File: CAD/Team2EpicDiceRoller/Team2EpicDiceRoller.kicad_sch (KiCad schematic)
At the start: 64 parts, among them J1 Conn_02x03_Odd_Even, J2 Conn_01x16, J3 Barrel_Jack, Q1 BSS138, SW1 SW_Toggle_SPDT, SW2 Tilt_Switch, SW3 SW_Power, SW4 RotaryEncoder_Switch, SW5 SW_LeftMenu, SW6 SW_MidMenu, SW7 SW_Reset, SW8 SW_RightMenu, U1 MC34063AD, U2 74HC14, U3 MC34063AD, U4 ATmega328P-P, Y1 Crystal_16MHz

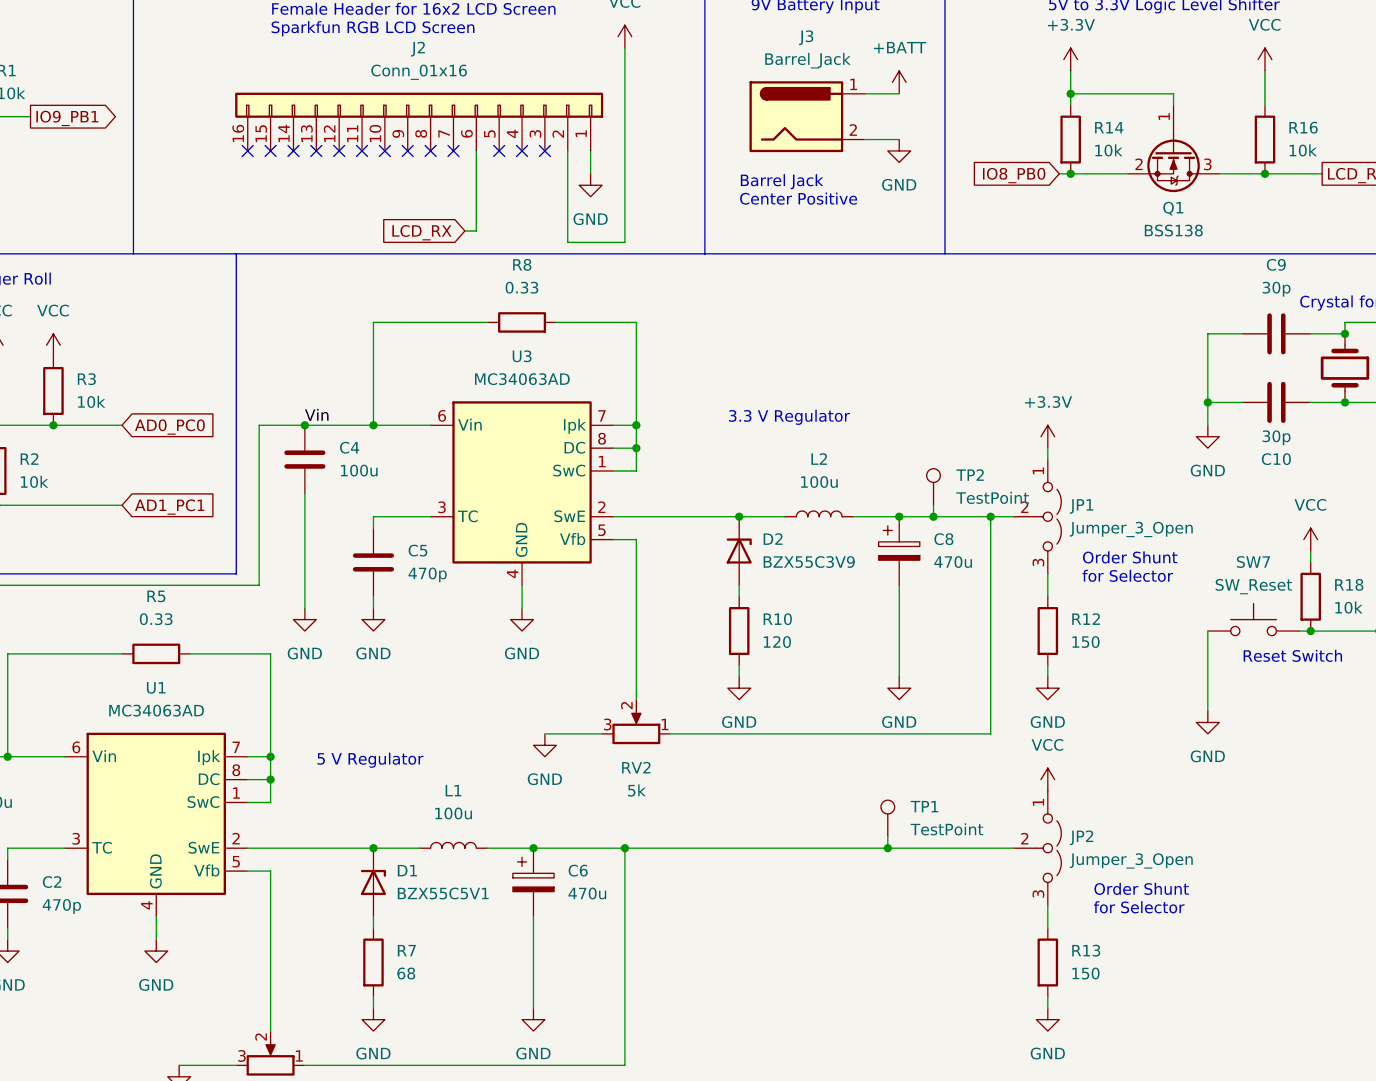
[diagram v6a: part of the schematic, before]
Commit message: Added mounting holes for the standoffs
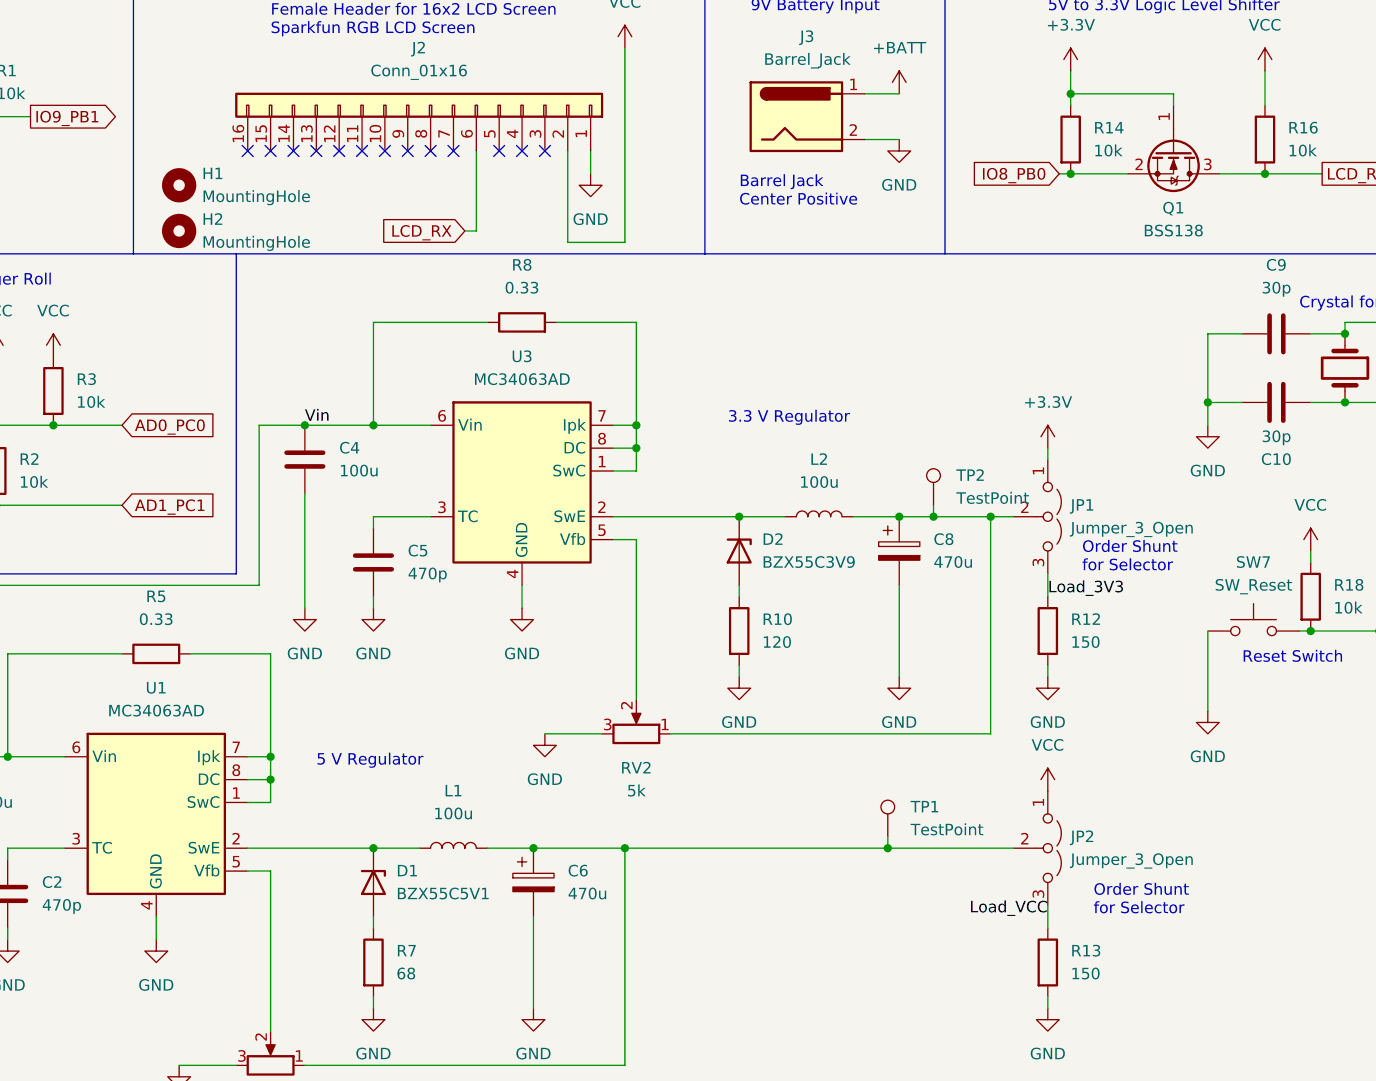
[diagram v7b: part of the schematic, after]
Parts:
- added H1, H2: MountingHole, MountingHole:MountingHole_3.2mm_M3, symbol Mechanical:MountingHole
- J2: footprint Connector_PinSocket_2.54mm:PinSocket_1x16_P2.54mm_Vertical -> Library:PinSocket_1x16_P2.54mm_Vertical_LCD
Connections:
- net Load_VCC: now reaches JP2.3 (B), R13.1
- net Load_3V3: now reaches JP1.3 (B), R12.1
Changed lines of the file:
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@@
     (effects (font (size 1.27 1.27)) (justify left bottom))
   )
-  (text "Order Shunt\nfor Selector" (at 158.75 137.16 0)
+  (text "Order Shunt\nfor Selector" (at 158.75 135.89 0)
     (effects (font (size 1.27 1.27)) (justify left bottom))
   )
@@
   (label "LeftDebn" (at 130.81 30.48 90)
     (effects (font (size 1.27 1.27)) (justify left bottom))
+  )
+  (label "Load_3V3" (at 154.94 138.43 0)
+    (effects (font (size 1.27 1.27)) (justify left bottom))
+  )
+  (label "Load_VCC" (at 154.94 173.99 180)
+    (effects (font (size 1.27 1.27)) (justify right bottom))
   )
   (label "MidDebn" (at 191.77 30.48 90)
@@
     (pin "1")
     (pin "2")
+  )
+  (symbol (lib_id "Mechanical:MountingHole") (at 58.42 92.71 0) (unit 1)
+    (in_bom yes) (on_board yes) (fields_autoplaced)
+    (property "Reference" "H1" (id 0) (at 60.96 91.4399 0)
+      (effects (font (size 1.27 1.27)) (justify left))
+    )
+    (property "Value" "MountingHole" (id 1) (at 60.96 93.9799 0)
+      (effects (font (size 1.27 1.27)) (justify left))
+    )
+    (property "Footprint" "MountingHole:MountingHole_3.2mm_M3" (id 2) (at 58.42 92.71 0)
+      (effects (font (size 1.27 1.27)) hide)
+    )
+    (property "Datasheet" "~" (id 3) (at 58.42 92.71 0)
+      (effects (font (size 1.27 1.27)) hide)
+    )
+  )
+  (symbol (lib_id "Mechanical:MountingHole") (at 58.42 97.79 0) (unit 1)
+    (in_bom yes) (on_board yes) (fields_autoplaced)
+    (property "Reference" "H2" (id 0) (at 60.96 96.5199 0)
+      (effects (font (size 1.27 1.27)) (justify left))
+    )
+    (property "Value" "MountingHole" (id 1) (at 60.96 99.0599 0)
+      (effects (font (size 1.27 1.27)) (justify left))
+    )
+    (property "Footprint" "MountingHole:MountingHole_3.2mm_M3" (id 2) (at 58.42 97.79 0)
+      (effects (font (size 1.27 1.27)) hide)
+    )
+    (property "Datasheet" "~" (id 3) (at 58.42 97.79 0)
+      (effects (font (size 1.27 1.27)) hide)
+    )
   )
   (symbol (lib_id "Device:R") (at 19.05 26.67 180) (unit 1)
@@
     (property "Reference" "J2" (id 0) (at 85.09 77.47 90))
     (property "Value" "Conn_01x16" (id 1) (at 85.09 80.01 90))
-    (property "Footprint" "Connector_PinSocket_2.54mm:PinSocket_1x16_P2.54mm_Vertical" (id 2) (at 86.36 83.82 0)
+    (property "Footprint" "Library:PinSocket_1x16_P2.54mm_Vertical_LCD" (id 2) (at 86.36 83.82 0)
       (effects (font (size 1.27 1.27)) hide)
     )
@@
       (reference "D2") (unit 1) (value "BZX55C3V9") (footprint "Diode_THT:D_DO-35_SOD27_P7.62mm_Horizontal")
     )
+    (path "/89d096c1-e2f8-495f-b214-91c56d1cbee4"
+      (reference "H1") (unit 1) (value "MountingHole") (footprint "MountingHole:MountingHole_3.2mm_M3")
+    )
+    (path "/f32266d9-a3df-4950-8cf5-205f2086c5fb"
+      (reference "H2") (unit 1) (value "MountingHole") (footprint "MountingHole:MountingHole_3.2mm_M3")
+    )
     (path "/97500fde-4c78-42dd-ab07-3c6ad623f25a"
       (reference "J1") (unit 1) (value "Conn_02x03_Odd_Even") (footprint "Connector_PinSocket_2.54mm:PinSocket_2x03_P2.54mm_Vertical")
     )
-    (path "/0e7ae0e4-6b41-4652-9a95-db205a649e5e"
-      (reference "J2") (unit 1) (value "Conn_01x16") (footprint "Connector_PinSocket_2.54mm:PinSocket_1x16_P2.54mm_Vertical")
+    (path "/774bab15-cccc-4eaf-817c-899e3423a665"
+      (reference "J2") (unit 1) (value "Conn_01x16") (footprint "Library:PinSocket_1x16_P2.54mm_Vertical_LCD")
     )
     (path "/a22f0e59-c995-4a77-b01f-895393d42f53"

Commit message: Newer version
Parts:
- added TPG1, TPG2: TestPointGND, TestPoint:TestPoint_Pad_D2.0mm, symbol Connector:TestPoint
- TP1: value TestPoint -> TestPointVCC
- TP2: value TestPoint -> TestPoint3V3
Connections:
- net GND: now also TPG1.1, TPG2.1
- net IO5_PD5: now also U2.2; no longer U2.6
- net IO7_PD7: now also U2.6; no longer U2.2
- net LeftDebn: now also U2.1; no longer U2.5
- net RigDebn: now also U2.5; no longer U2.1
- net VCC: now also C6.1, JP2.2 (C), L1.2, RV1.1, TP1.1
- net 3V3: now reaches C8.1, JP1.2 (C), L2.2, RV2.1, TP2.1
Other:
- moved on the sheet: U2A, U2C
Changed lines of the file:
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@@
   (junction (at 142.24 129.54) (diameter 0) (color 0 0 0 0))
   (junction (at 148.59 129.54) (diameter 0) (color 0 0 0 0))
+  (junction (at 154.94 147.32) (diameter 0) (color 0 0 0 0))
+  (junction (at 154.94 184.15) (diameter 0) (color 0 0 0 0))
   (junction (at 157.48 82.55) (diameter 0) (color 0 0 0 0))
   (junction (at 157.48 91.44) (diameter 0) (color 0 0 0 0))
@@
     (effects (font (size 1.27 1.27)) (justify left bottom))
   )
+  (label "VCC" (at 130.81 166.37 0)
+    (effects (font (size 1.27 1.27)) (justify left bottom))
+  )
+  (label "3V3" (at 138.43 129.54 0)
+    (effects (font (size 1.27 1.27)) (justify left bottom))
+  )
   (label "Load_3V3" (at 154.94 138.43 0)
     (effects (font (size 1.27 1.27)) (justify left bottom))
@@
       (effects (font (size 1.27 1.27)) (justify left))
     )
-    (property "Value" "TestPoint" (id 1) (at 139.7 164.3379 0)
+    (property "Value" "TestPointVCC" (id 1) (at 139.7 164.3379 0)
       (effects (font (size 1.27 1.27)) (justify left))
     )
@@
   )
   (symbol (lib_id "Connector:TestPoint") (at 142.24 128.27 0) (unit 1)
-    (in_bom yes) (on_board yes) (fields_autoplaced)
+    (in_bom yes) (on_board yes)
     (property "Reference" "TP2" (id 0) (at 144.78 124.9679 0)
       (effects (font (size 1.27 1.27)) (justify left))
     )
-    (property "Value" "TestPoint" (id 1) (at 144.78 127.5079 0)
+    (property "Value" "TestPoint3V3" (id 1) (at 142.24 127.5079 0)
       (effects (font (size 1.27 1.27)) (justify left))
     )
@@
     (pin "1")
   )
+  (symbol (lib_id "Connector:TestPoint") (at 154.94 147.32 270) (unit 1)
+    (in_bom yes) (on_board yes) (fields_autoplaced)
+    (property "Reference" "TPG1" (id 0) (at 160.02 146.0499 90)
+      (effects (font (size 1.27 1.27)) (justify left))
+    )
+    (property "Value" "TestPointGND" (id 1) (at 160.02 148.5899 90)
+      (effects (font (size 1.27 1.27)) (justify left))
+    )
+    (property "Footprint" "TestPoint:TestPoint_Pad_D2.0mm" (id 2) (at 154.94 152.4 0)
+      (effects (font (size 1.27 1.27)) hide)
+    )
+    (property "Datasheet" "~" (id 3) (at 154.94 152.4 0)
+      (effects (font (size 1.27 1.27)) hide)
+    )
+    (pin "1")
+  )
+  (symbol (lib_id "Connector:TestPoint") (at 154.94 184.15 270) (unit 1)
+    (in_bom yes) (on_board yes) (fields_autoplaced)
+    (property "Reference" "TPG2" (id 0) (at 160.02 182.8799 90)
+      (effects (font (size 1.27 1.27)) (justify left))
+    )
+    (property "Value" "TestPointGND" (id 1) (at 160.02 185.4199 90)
+      (effects (font (size 1.27 1.27)) (justify left))
+    )
+    (property "Footprint" "TestPoint:TestPoint_Pad_D2.0mm" (id 2) (at 154.94 189.23 0)
+      (effects (font (size 1.27 1.27)) hide)
+    )
+    (property "Datasheet" "~" (id 3) (at 154.94 189.23 0)
+      (effects (font (size 1.27 1.27)) hide)
+    )
+    (pin "1")
+  )
   (symbol (lib_id "power:GND") (at 16.51 128.27 0) (unit 1)
     (in_bom yes) (on_board yes) (fields_autoplaced)
@@
     (pin "9")
   )
-  (symbol (lib_id "74xx:74HC14") (at 143.51 30.48 0) (unit 3)
+  (symbol (lib_id "74xx:74HC14") (at 143.51 30.48 0) (unit 1)
     (in_bom yes) (on_board yes) (fields_autoplaced)
     (property "Reference" "U2" (id 0) (at 143.51 21.59 0))
@@
       (effects (font (size 1.27 1.27)) hide)
     )
-    (pin "5")
-    (pin "6")
+    (pin "1")
+    (pin "2")
   )
   (symbol (lib_id "74xx:74HC14") (at 143.51 54.61 0) (unit 5)
@@
     (pin "4")
   )
-  (symbol (lib_id "74xx:74HC14") (at 262.89 30.48 0) (unit 1)
+  (symbol (lib_id "74xx:74HC14") (at 262.89 30.48 0) (unit 3)
     (in_bom yes) (on_board yes) (fields_autoplaced)
     (property "Reference" "U2" (id 0) (at 262.89 21.59 0))
@@
       (effects (font (size 1.27 1.27)) hide)
     )
-    (pin "1")
-    (pin "2")
+    (pin "5")
+    (pin "6")
   )
   (symbol (lib_name "RotaryEncoder_Switch_1") (lib_id "Device:RotaryEncoder_Switch") (at 36.83 33.02 0) (unit 1)
@@
     )
     (path "/7d1ff827-9479-427e-852e-01ec466ff6f9"
-      (reference "TP1") (unit 1) (value "TestPoint") (footprint "TestPoint:TestPoint_Pad_D2.0mm")
+      (reference "TP1") (unit 1) (value "TestPointVCC") (footprint "TestPoint:TestPoint_Pad_D2.0mm")
     )
     (path "/9423c47e-8566-4af8-ad8a-b85648689249"
-      (reference "TP2") (unit 1) (value "TestPoint") (footprint "TestPoint:TestPoint_Pad_D2.0mm")
+      (reference "TP2") (unit 1) (value "TestPoint3V3") (footprint "TestPoint:TestPoint_Pad_D2.0mm")
+    )
+    (path "/d4b4fe16-5ecf-42ce-9bfe-1e998d952a73"
+      (reference "TPG1") (unit 1) (value "TestPointGND") (footprint "TestPoint:TestPoint_Pad_D2.0mm")
+    )
+    (path "/b185729d-96f1-4955-a2d9-ad531a37265a"
+      (reference "TPG2") (unit 1) (value "TestPointGND") (footprint "TestPoint:TestPoint_Pad_D2.0mm")
     )
     (path "/6ac96d5f-5167-47fa-b9d4-15bdec4bb4fd"
